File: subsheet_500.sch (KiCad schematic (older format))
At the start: 48 parts, among them J500 DM-15S — JOY0, J501 DM-15S — JOY1, U513 LM556_DUAL_TIMER_PHY, U514 LM556_DUAL_TIMER_PHY

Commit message: Removed T-filters
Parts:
- removed L506, L507, L509, L510, L511, L512, L513, L514, L515, L516, L517, L518, L519, L520, L521, L522, L523, L524, L525, L526, L527: EMI_Filter_LCL, commons_passives_THT:Passive_THT_EMI_filter_W5.08mm_L7.62mm, symbol Device:EMI_Filter_LCL
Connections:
- net labels removed: j0_1, j0_10, j0_11, j0_12, j0_13, j0_14, j0_2, j0_3, j0_4, j0_6, j0_7, j1_1, j1_10, j1_11, j1_12, j1_13, j1_14, j1_2, j1_3, j1_4, j1_6, j1_7
- wire segments 154 -> 111
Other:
- moved on the sheet: C526, C527, C532, C533, C539, C540, C548, C549, C554, C555, J501, L500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

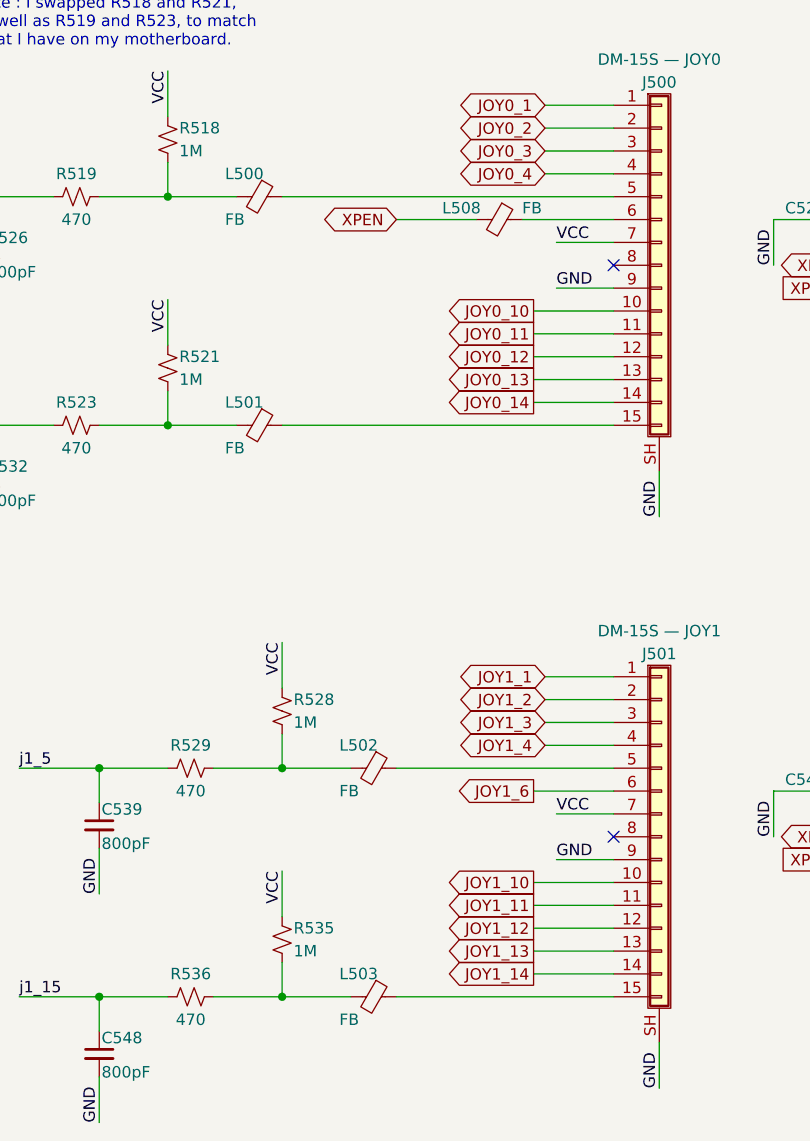
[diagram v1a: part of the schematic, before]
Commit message: Resolves #11 : Use the reference 'FB?' for the ferrite beads
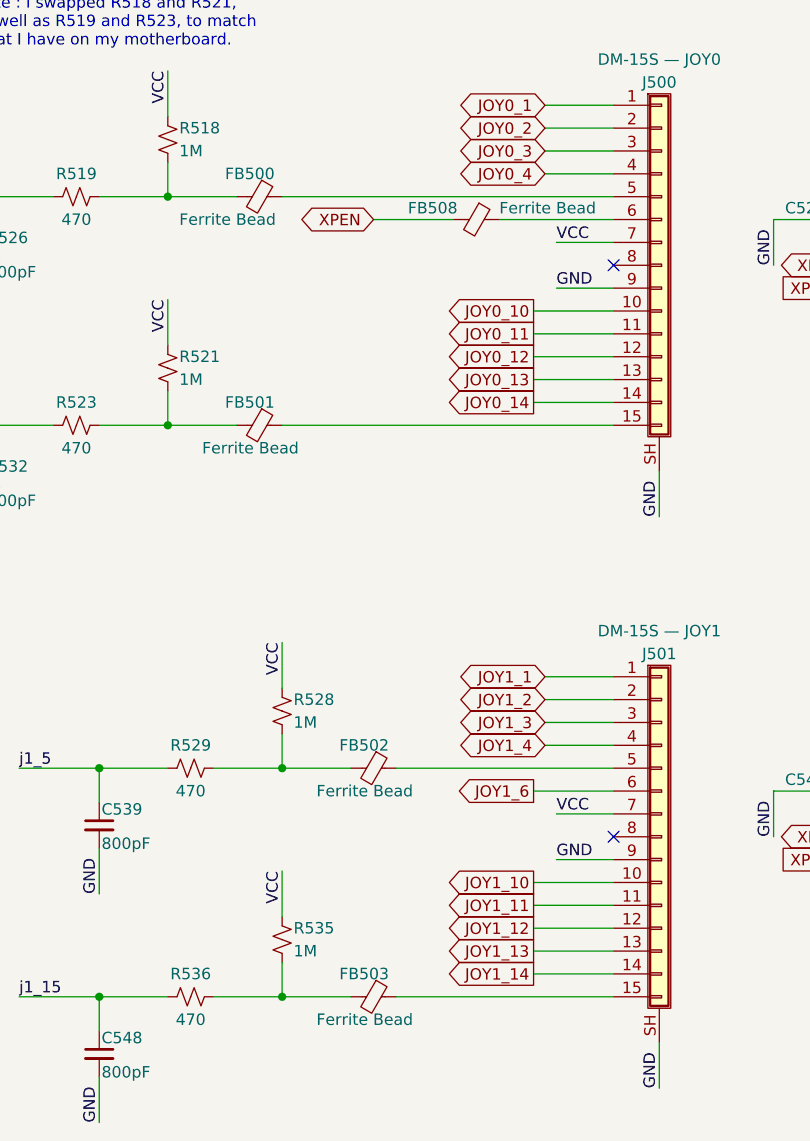
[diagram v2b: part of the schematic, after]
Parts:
- FB500: renamed from L500; value FB -> Ferrite Bead
- FB501: renamed from L501; value FB -> Ferrite Bead
- FB502: renamed from L502; value FB -> Ferrite Bead
- FB503: renamed from L503; value FB -> Ferrite Bead
- FB508: renamed from L508; value FB -> Ferrite Bead
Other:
- moved on the sheet: FB508
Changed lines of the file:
@@
 GND
-Wire Wire Line
-	3250 1600 3650 1600
 Wire Wire Line
 	3400 1900 3650 1900
@@
 NoConn ~ 3650 4300
 $Comp
-L Device:Ferrite_Bead_Small L500
+L Device:Ferrite_Bead_Small FB500
 U 1 1 60CA63D1
 P 2100 1500
-F 0 "L500" V 2000 1350 50  0000 L CNN
-F 1 "FB" V 2200 1350 50  0000 L CNN
+F 0 "FB500" V 2000 1350 50  0000 L CNN
+F 1 "Ferrite Bead" V 2200 1150 50  0000 L CNN
 F 2 "commons_passives_THT:Passive_THT_ferrite_bead_W3.81mm_L15.24mm" V 2030 1500 50  0001 C CNN
 F 3 "~" H 2100 1500 50  0001 C CNN
@@
 $EndComp
 $Comp
-L Device:Ferrite_Bead_Small L501
+L Device:Ferrite_Bead_Small FB501
 U 1 1 60CA7646
 P 2100 2500
-F 0 "L501" V 2000 2350 50  0000 L CNN
-F 1 "FB" V 2200 2350 50  0000 L CNN
+F 0 "FB501" V 2000 2350 50  0000 L CNN
+F 1 "Ferrite Bead" V 2200 2250 50  0000 L CNN
 F 2 "commons_passives_THT:Passive_THT_ferrite_bead_W3.81mm_L15.24mm" V 2030 2500 50  0001 C CNN
 F 3 "~" H 2100 2500 50  0001 C CNN
@@
 $EndComp
 $Comp
-L Device:Ferrite_Bead_Small L502
+L Device:Ferrite_Bead_Small FB502
 U 1 1 60CA80BE
 P 2600 4000
-F 0 "L502" V 2500 3850 50  0000 L CNN
-F 1 "FB" V 2700 3850 50  0000 L CNN
+F 0 "FB502" V 2500 3850 50  0000 L CNN
+F 1 "Ferrite Bead" V 2700 3750 50  0000 L CNN
 F 2 "commons_passives_THT:Passive_THT_ferrite_bead_W3.81mm_L15.24mm" V 2530 4000 50  0001 C CNN
 F 3 "~" H 2600 4000 50  0001 C CNN
@@
 $EndComp
 $Comp
-L Device:Ferrite_Bead_Small L503
+L Device:Ferrite_Bead_Small FB503
 U 1 1 60CA88E0
 P 2600 5000
-F 0 "L503" V 2500 4850 50  0000 L CNN
-F 1 "FB" V 2700 4850 50  0000 L CNN
+F 0 "FB503" V 2500 4850 50  0000 L CNN
+F 1 "Ferrite Bead" V 2700 4750 50  0000 L CNN
 F 2 "commons_passives_THT:Passive_THT_ferrite_bead_W3.81mm_L15.24mm" V 2530 5000 50  0001 C CNN
 F 3 "~" H 2600 5000 50  0001 C CNN
@@
 Text GLabel 3300 2400 0    50   Output ~ 0
 JOY0_14
-$Comp
-L Device:Ferrite_Bead_Small L508
-U 1 1 60DFED5B
-P 3150 1600
-F 0 "L508" V 3100 1350 50  0000 L CNN
-F 1 "FB" V 3100 1700 50  0000 L CNN
-F 2 "commons_passives_THT:Passive_THT_ferrite_bead_W3.81mm_L15.24mm" V 3080 1600 50  0001 C CNN
-F 3 "~" H 3150 1600 50  0001 C CNN
-	1    3150 1600
-	0    1    1    0
-$EndComp
-Text GLabel 2700 1600 0    50   BiDi ~ 0
+Text GLabel 2600 1600 0    50   BiDi ~ 0
 XPEN
 Text GLabel 3350 3600 0    50   BiDi ~ 0
@@
 	2200 2500 3650 2500
 Wire Wire Line
-	3050 1600 2700 1600
+	2950 1600 2600 1600
 Wire Wire Line
 	3400 1700 3650 1700
@@
 Wire Wire Line
 	2700 5000 3650 5000
+$Comp
+L Device:Ferrite_Bead_Small FB508
+U 1 1 60DFED5B
+P 3050 1600
+F 0 "FB508" V 3000 1300 50  0000 L CNN
+F 1 "Ferrite Bead" V 3000 1700 50  0000 L CNN
+F 2 "commons_passives_THT:Passive_THT_ferrite_bead_W3.81mm_L15.24mm" V 2980 1600 50  0001 C CNN
+F 3 "~" H 3050 1600 50  0001 C CNN
+	1    3050 1600
+	0    1    1    0
+$EndComp
+Wire Wire Line
+	3150 1600 3650 1600
 $EndSCHEMATC

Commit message: Resolves #13 : assign 1206 hand-solder footprints to resistors
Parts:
- R518, R519, R521, R523, R528, R529, R535, R536: footprint commons_passives_THT:Passive_THT_resistor_W2.54mm_L12.70mm -> Resistor_SMD:R_1206_3216Metric_Pad1.30x1.75mm_HandSolder
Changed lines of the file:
@@
 F 0 "R521" H 1750 2300 50  0000 L CNN
 F 1 "1M" H 1750 2200 50  0000 L CNN
-F 2 "commons_passives_THT:Passive_THT_resistor_W2.54mm_L12.70mm" H 1700 2250 50  0001 C CNN
+F 2 "Resistor_SMD:R_1206_3216Metric_Pad1.30x1.75mm_HandSolder" H 1700 2250 50  0001 C CNN
 F 3 "~" H 1700 2250 50  0001 C CNN
 	1    1700 2250
@@
 F 0 "R518" H 1750 1300 50  0000 L CNN
 F 1 "1M" H 1750 1200 50  0000 L CNN
-F 2 "commons_passives_THT:Passive_THT_resistor_W2.54mm_L12.70mm" H 1700 1250 50  0001 C CNN
+F 2 "Resistor_SMD:R_1206_3216Metric_Pad1.30x1.75mm_HandSolder" H 1700 1250 50  0001 C CNN
 F 3 "~" H 1700 1250 50  0001 C CNN
 	1    1700 1250
@@
 F 0 "R528" H 2250 3800 50  0000 L CNN
 F 1 "1M" H 2250 3700 50  0000 L CNN
-F 2 "commons_passives_THT:Passive_THT_resistor_W2.54mm_L12.70mm" H 2200 3750 50  0001 C CNN
+F 2 "Resistor_SMD:R_1206_3216Metric_Pad1.30x1.75mm_HandSolder" H 2200 3750 50  0001 C CNN
 F 3 "~" H 2200 3750 50  0001 C CNN
 	1    2200 3750
@@
 F 0 "R535" H 2250 4800 50  0000 L CNN
 F 1 "1M" H 2250 4700 50  0000 L CNN
-F 2 "commons_passives_THT:Passive_THT_resistor_W2.54mm_L12.70mm" H 2200 4750 50  0001 C CNN
+F 2 "Resistor_SMD:R_1206_3216Metric_Pad1.30x1.75mm_HandSolder" H 2200 4750 50  0001 C CNN
 F 3 "~" H 2200 4750 50  0001 C CNN
 	1    2200 4750
@@
 F 0 "R523" V 1200 2500 50  0000 C CNN
 F 1 "470" V 1400 2500 50  0000 C CNN
-F 2 "commons_passives_THT:Passive_THT_resistor_W2.54mm_L12.70mm" H 1300 2500 50  0001 C CNN
+F 2 "Resistor_SMD:R_1206_3216Metric_Pad1.30x1.75mm_HandSolder" H 1300 2500 50  0001 C CNN
 F 3 "~" H 1300 2500 50  0001 C CNN
 	1    1300 2500
@@
 F 0 "R519" V 1200 1500 50  0000 C CNN
 F 1 "470" V 1400 1500 50  0000 C CNN
-F 2 "commons_passives_THT:Passive_THT_resistor_W2.54mm_L12.70mm" H 1300 1500 50  0001 C CNN
+F 2 "Resistor_SMD:R_1206_3216Metric_Pad1.30x1.75mm_HandSolder" H 1300 1500 50  0001 C CNN
 F 3 "~" H 1300 1500 50  0001 C CNN
 	1    1300 1500
@@
 F 0 "R529" V 1700 4000 50  0000 C CNN
 F 1 "470" V 1900 4000 50  0000 C CNN
-F 2 "commons_passives_THT:Passive_THT_resistor_W2.54mm_L12.70mm" H 1800 4000 50  0001 C CNN
+F 2 "Resistor_SMD:R_1206_3216Metric_Pad1.30x1.75mm_HandSolder" H 1800 4000 50  0001 C CNN
 F 3 "~" H 1800 4000 50  0001 C CNN
 	1    1800 4000
@@
 F 0 "R536" V 1700 5000 50  0000 C CNN
 F 1 "470" V 1900 5000 50  0000 C CNN
-F 2 "commons_passives_THT:Passive_THT_resistor_W2.54mm_L12.70mm" H 1800 5000 50  0001 C CNN
+F 2 "Resistor_SMD:R_1206_3216Metric_Pad1.30x1.75mm_HandSolder" H 1800 5000 50  0001 C CNN
 F 3 "~" H 1800 5000 50  0001 C CNN
 	1    1800 5000

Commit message: Resolves #8 : Assign 1206 hand-solder footprints to non polarized capacitors
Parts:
- C526, C532, C539, C548: footprint commons_passives_THT:Passive_THT_capacitor_ceramic_radial_W5.08mm_L6.35mm_X11.43mm -> Capacitor_SMD:C_1206_3216Metric_Pad1.33x1.80mm_HandSolder
- C527, C533, C540, C549: footprint commons_passives_THT:Passive_THT_capacitor_W2.54mm_L10.16mm -> Capacitor_SMD:C_1206_3216Metric_Pad1.33x1.80mm_HandSolder
- C554, C555: footprint commons_passives_THT:Passive_THT_capacitor_mlcc_W2.54mm_L7.62mm -> Capacitor_SMD:C_1206_3216Metric_Pad1.33x1.80mm_HandSolder
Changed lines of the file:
@@
 F 0 "C532" H 910 2820 50  0000 L CNN
 F 1 "800pF" H 910 2670 50  0000 L CNN
-F 2 "commons_passives_THT:Passive_THT_capacitor_ceramic_radial_W5.08mm_L6.35mm_X11.43mm" H 900 2750 50  0001 C CNN
+F 2 "Capacitor_SMD:C_1206_3216Metric_Pad1.33x1.80mm_HandSolder" H 900 2750 50  0001 C CNN
 F 3 "~" H 900 2750 50  0001 C CNN
 	1    900  2750
@@
 F 0 "C526" H 910 1820 50  0000 L CNN
 F 1 "800pF" H 910 1670 50  0000 L CNN
-F 2 "commons_passives_THT:Passive_THT_capacitor_ceramic_radial_W5.08mm_L6.35mm_X11.43mm" H 900 1750 50  0001 C CNN
+F 2 "Capacitor_SMD:C_1206_3216Metric_Pad1.33x1.80mm_HandSolder" H 900 1750 50  0001 C CNN
 F 3 "~" H 900 1750 50  0001 C CNN
 	1    900  1750
@@
 F 0 "C539" H 1410 4320 50  0000 L CNN
 F 1 "800pF" H 1410 4170 50  0000 L CNN
-F 2 "commons_passives_THT:Passive_THT_capacitor_ceramic_radial_W5.08mm_L6.35mm_X11.43mm" H 1400 4250 50  0001 C CNN
+F 2 "Capacitor_SMD:C_1206_3216Metric_Pad1.33x1.80mm_HandSolder" H 1400 4250 50  0001 C CNN
 F 3 "~" H 1400 4250 50  0001 C CNN
 	1    1400 4250
@@
 F 0 "C548" H 1410 5320 50  0000 L CNN
 F 1 "800pF" H 1410 5170 50  0000 L CNN
-F 2 "commons_passives_THT:Passive_THT_capacitor_ceramic_radial_W5.08mm_L6.35mm_X11.43mm" H 1400 5250 50  0001 C CNN
+F 2 "Capacitor_SMD:C_1206_3216Metric_Pad1.33x1.80mm_HandSolder" H 1400 5250 50  0001 C CNN
 F 3 "~" H 1400 5250 50  0001 C CNN
 	1    1400 5250
@@
 F 0 "C527" V 4600 1350 50  0000 L CNN
 F 1 "0.01uF" V 4600 1650 50  0000 L CNN
-F 2 "commons_passives_THT:Passive_THT_capacitor_W2.54mm_L10.16mm" H 4650 1600 50  0001 C CNN
+F 2 "Capacitor_SMD:C_1206_3216Metric_Pad1.33x1.80mm_HandSolder" H 4650 1600 50  0001 C CNN
 F 3 "~" H 4650 1600 50  0001 C CNN
 	1    4650 1600
@@
 F 0 "C533" V 7250 1450 50  0000 L CNN
 F 1 "0.01uF" V 7250 1750 50  0000 L CNN
-F 2 "commons_passives_THT:Passive_THT_capacitor_W2.54mm_L10.16mm" H 7300 1700 50  0001 C CNN
+F 2 "Capacitor_SMD:C_1206_3216Metric_Pad1.33x1.80mm_HandSolder" H 7300 1700 50  0001 C CNN
 F 3 "~" H 7300 1700 50  0001 C CNN
 	1    7300 1700
@@
 F 0 "C540" V 4600 3850 50  0000 L CNN
 F 1 "0.01uF" V 4600 4150 50  0000 L CNN
-F 2 "commons_passives_THT:Passive_THT_capacitor_W2.54mm_L10.16mm" H 4650 4100 50  0001 C CNN
+F 2 "Capacitor_SMD:C_1206_3216Metric_Pad1.33x1.80mm_HandSolder" H 4650 4100 50  0001 C CNN
 F 3 "~" H 4650 4100 50  0001 C CNN
 	1    4650 4100
@@
 F 0 "C549" V 7350 4250 50  0000 L CNN
 F 1 "0.01uF" V 7350 3900 50  0000 L CNN
-F 2 "commons_passives_THT:Passive_THT_capacitor_W2.54mm_L10.16mm" H 7300 4200 50  0001 C CNN
+F 2 "Capacitor_SMD:C_1206_3216Metric_Pad1.33x1.80mm_HandSolder" H 7300 4200 50  0001 C CNN
 F 3 "~" H 7300 4200 50  0001 C CNN
 	1    7300 4200
@@
 F 0 "C554" H 6825 2650 50  0000 L CNN
 F 1 "0.1uF" H 6825 2450 50  0000 L CNN
-F 2 "commons_passives_THT:Passive_THT_capacitor_mlcc_W2.54mm_L7.62mm" H 6838 2400 50  0001 C CNN
+F 2 "Capacitor_SMD:C_1206_3216Metric_Pad1.33x1.80mm_HandSolder" H 6838 2400 50  0001 C CNN
 F 3 "~" H 6800 2550 50  0001 C CNN
 	1    6800 2550
@@
 F 0 "C555" H 6825 5150 50  0000 L CNN
 F 1 "0.1uF" H 6825 4950 50  0000 L CNN
-F 2 "commons_passives_THT:Passive_THT_capacitor_mlcc_W2.54mm_L7.62mm" H 6838 4900 50  0001 C CNN
+F 2 "Capacitor_SMD:C_1206_3216Metric_Pad1.33x1.80mm_HandSolder" H 6838 4900 50  0001 C CNN
 F 3 "~" H 6800 5050 50  0001 C CNN
 	1    6800 5050

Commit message: Resolves #14 : assign smd footprints for ferrite beads
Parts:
- FB500, FB501, FB502, FB503, FB508: footprint commons_passives_THT:Passive_THT_ferrite_bead_W3.81mm_L15.24mm -> Inductor_SMD:L_1206_3216Metric_Pad1.22x1.90mm_HandSolder
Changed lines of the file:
@@
 F 0 "FB500" V 2000 1350 50  0000 L CNN
 F 1 "Ferrite Bead" V 2200 1150 50  0000 L CNN
-F 2 "commons_passives_THT:Passive_THT_ferrite_bead_W3.81mm_L15.24mm" V 2030 1500 50  0001 C CNN
+F 2 "Inductor_SMD:L_1206_3216Metric_Pad1.22x1.90mm_HandSolder" V 2030 1500 50  0001 C CNN
 F 3 "~" H 2100 1500 50  0001 C CNN
 	1    2100 1500
@@
 F 0 "FB501" V 2000 2350 50  0000 L CNN
 F 1 "Ferrite Bead" V 2200 2250 50  0000 L CNN
-F 2 "commons_passives_THT:Passive_THT_ferrite_bead_W3.81mm_L15.24mm" V 2030 2500 50  0001 C CNN
+F 2 "Inductor_SMD:L_1206_3216Metric_Pad1.22x1.90mm_HandSolder" V 2030 2500 50  0001 C CNN
 F 3 "~" H 2100 2500 50  0001 C CNN
 	1    2100 2500
@@
 F 0 "FB502" V 2500 3850 50  0000 L CNN
 F 1 "Ferrite Bead" V 2700 3750 50  0000 L CNN
-F 2 "commons_passives_THT:Passive_THT_ferrite_bead_W3.81mm_L15.24mm" V 2530 4000 50  0001 C CNN
+F 2 "Inductor_SMD:L_1206_3216Metric_Pad1.22x1.90mm_HandSolder" V 2530 4000 50  0001 C CNN
 F 3 "~" H 2600 4000 50  0001 C CNN
 	1    2600 4000
@@
 F 0 "FB503" V 2500 4850 50  0000 L CNN
 F 1 "Ferrite Bead" V 2700 4750 50  0000 L CNN
-F 2 "commons_passives_THT:Passive_THT_ferrite_bead_W3.81mm_L15.24mm" V 2530 5000 50  0001 C CNN
+F 2 "Inductor_SMD:L_1206_3216Metric_Pad1.22x1.90mm_HandSolder" V 2530 5000 50  0001 C CNN
 F 3 "~" H 2600 5000 50  0001 C CNN
 	1    2600 5000
@@
 F 0 "FB508" V 3000 1300 50  0000 L CNN
 F 1 "Ferrite Bead" V 3000 1700 50  0000 L CNN
-F 2 "commons_passives_THT:Passive_THT_ferrite_bead_W3.81mm_L15.24mm" V 2980 1600 50  0001 C CNN
+F 2 "Inductor_SMD:L_1206_3216Metric_Pad1.22x1.90mm_HandSolder" V 2980 1600 50  0001 C CNN
 F 3 "~" H 3050 1600 50  0001 C CNN
 	1    3050 1600
